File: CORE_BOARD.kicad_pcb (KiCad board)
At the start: 4 copper layers, 25 x 18 mm, 4 parts

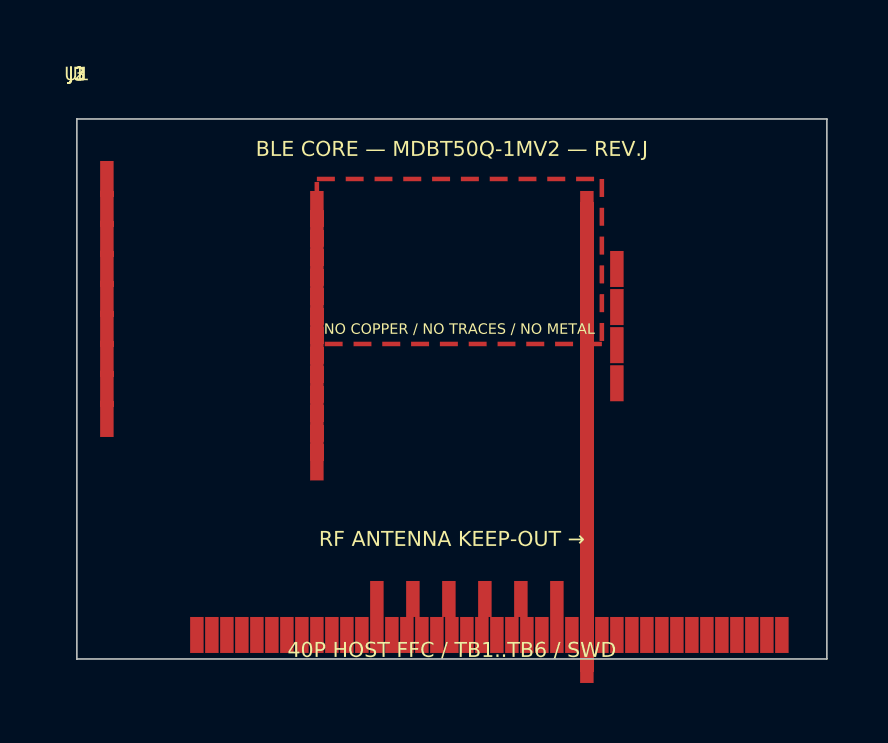
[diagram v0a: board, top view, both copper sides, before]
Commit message: Finalize CORE host FFC as 24P
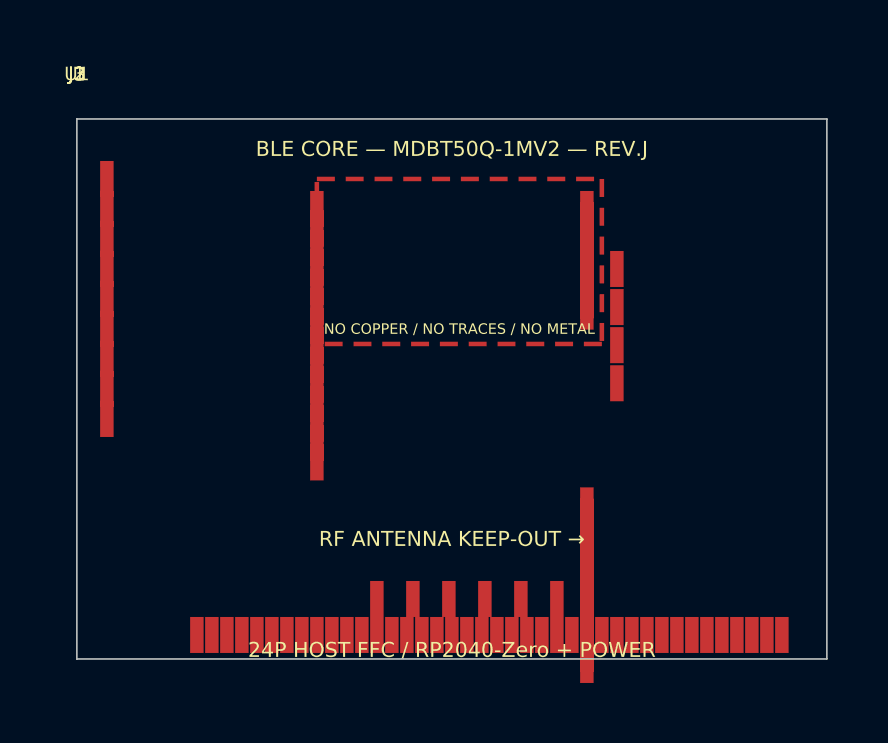
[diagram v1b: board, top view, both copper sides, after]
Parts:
- J1: footprint FH34SRJ-40S-0.5SH(50) -> FH34SRJ-24S-0.5SH(50)
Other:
- board text added: "24P HOST FFC / RP2040-Zero + POWER"
- board text removed: "40P HOST FFC / TB1..TB6 / SWD"
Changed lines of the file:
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@@
  (gr_rect (start 0 0) (end 25 18) (stroke (width 0.05) (type default)) (fill none) (layer "Edge.Cuts"))
  (gr_text "BLE CORE — MDBT50Q-1MV2 — REV.J" (at 12.5 1.0) (layer "F.SilkS") (effects (font (size 0.5 0.5) (thickness 0.1))))
- (gr_text "40P HOST FFC / TB1..TB6 / SWD" (at 12.5 17.7) (layer "F.SilkS") (effects (font (size 0.5 0.5) (thickness 0.1))))
+ (gr_text "24P HOST FFC / RP2040-Zero + POWER" (at 12.5 17.7) (layer "F.SilkS") (effects (font (size 0.5 0.5) (thickness 0.1))))
  (gr_text "RF ANTENNA KEEP-OUT →" (at 12.5 14.0) (layer "F.SilkS") (effects (font (size 0.5 0.5) (thickness 0.1))))
  (footprint "MDBT50Q-1MV2" (layer "F.Cu") (at 0 0)
@@
   (pad "23" smd rect (at 17 6.04) (size 0.45 1.2) (layers "F.Cu" "F.Paste" "F.Mask") (net 8 "GPIO4"))
   (pad "24" smd rect (at 17 6.42) (size 0.45 1.2) (layers "F.Cu" "F.Paste" "F.Mask") (net 9 "GPIO5"))
-  (pad "25" smd rect (at 17 6.8) (size 0.45 1.2) (layers "F.Cu" "F.Paste" "F.Mask") (net 10 "GPIO6"))
-  (pad "26" smd rect (at 17 7.18) (size 0.45 1.2) (layers "F.Cu" "F.Paste" "F.Mask") (net 11 "GPIO7"))
-  (pad "27" smd rect (at 17 7.5600000000000005) (size 0.45 1.2) (layers "F.Cu" "F.Paste" "F.Mask") (net 12 "GPIO8"))
-  (pad "28" smd rect (at 17 7.94) (size 0.45 1.2) (layers "F.Cu" "F.Paste" "F.Mask") (net 13 "3V3"))
-  (pad "29" smd rect (at 17 8.32) (size 0.45 1.2) (layers "F.Cu" "F.Paste" "F.Mask") (net 14 "GPIO9"))
-  (pad "30" smd rect (at 17 8.7) (size 0.45 1.2) (layers "F.Cu" "F.Paste" "F.Mask") (net 13 "3V3"))
-  (pad "31" smd rect (at 17 9.08) (size 0.45 1.2) (layers "F.Cu" "F.Paste" "F.Mask") (net 2 "NC"))
-  (pad "32" smd rect (at 17 9.46) (size 0.45 1.2) (layers "F.Cu" "F.Paste" "F.Mask") (net 15 "USB_VBUS"))
-  (pad "33" smd rect (at 17 9.84) (size 0.45 1.2) (layers "F.Cu" "F.Paste" "F.Mask") (net 1 "GND"))
-  (pad "34" smd rect (at 17 10.219999999999999) (size 0.45 1.2) (layers "F.Cu" "F.Paste" "F.Mask") (net 16 "USB_D-"))
-  (pad "35" smd rect (at 17 10.6) (size 0.45 1.2) (layers "F.Cu" "F.Paste" "F.Mask") (net 17 "USB_D+"))
-  (pad "36" smd rect (at 17 10.98) (size 0.45 1.2) (layers "F.Cu" "F.Paste" "F.Mask") (net 18 "GPIO11"))
-  (pad "37" smd rect (at 17 11.36) (size 0.45 1.2) (layers "F.Cu" "F.Paste" "F.Mask") (net 19 "GPIO10"))
-  (pad "38" smd rect (at 17 11.74) (size 0.45 1.2) (layers "F.Cu" "F.Paste" "F.Mask") (net 20 "GPIO13"))
-  (pad "39" smd rect (at 17 12.120000000000001) (size 0.45 1.2) (layers "F.Cu" "F.Paste" "F.Mask") (net 21 "GPIO12"))
-  (pad "40" smd rect (at 17 12.5) (size 0.45 1.2) (layers "F.Cu" "F.Paste" "F.Mask") (net 22 "RESET"))
   (pad "41" smd rect (at 17 12.88) (size 0.45 1.2) (layers "F.Cu" "F.Paste" "F.Mask") (net 23 "GPIO14"))
   (pad "42" smd rect (at 17 13.26) (size 0.45 1.2) (layers "F.Cu" "F.Paste" "F.Mask") (net 24 "GPIO15"))
@@
   (pad "61" smd rect (at 16.0 16) (size 0.45 1.2) (layers "F.Cu" "F.Paste" "F.Mask") (net 36 "TB6"))
  )
- (footprint "FH34SRJ-40S-0.5SH(50)" (layer "F.Cu") (at 0 0)
+ (footprint "FH34SRJ-24S-0.5SH(50)" (layer "F.Cu") (at 0 0)
   (fp_text reference "J1" (at 0 -1.5) (layer "F.SilkS") (effects (font (size 0.45 0.45) (thickness 0.08))))
   (pad "1" smd rect (at 4.0 17.2) (size 0.45 1.2) (layers "F.Cu" "F.Paste" "F.Mask") (net 3 "GPIO0"))
